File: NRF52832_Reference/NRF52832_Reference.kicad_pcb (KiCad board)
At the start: 2 copper layers, 47.5 x 35 mm, 24 parts, among them J1 MM8130-2600RA2, U1 NRF52810-QFAA, Y1 32MHz, Y2 32.768kHz

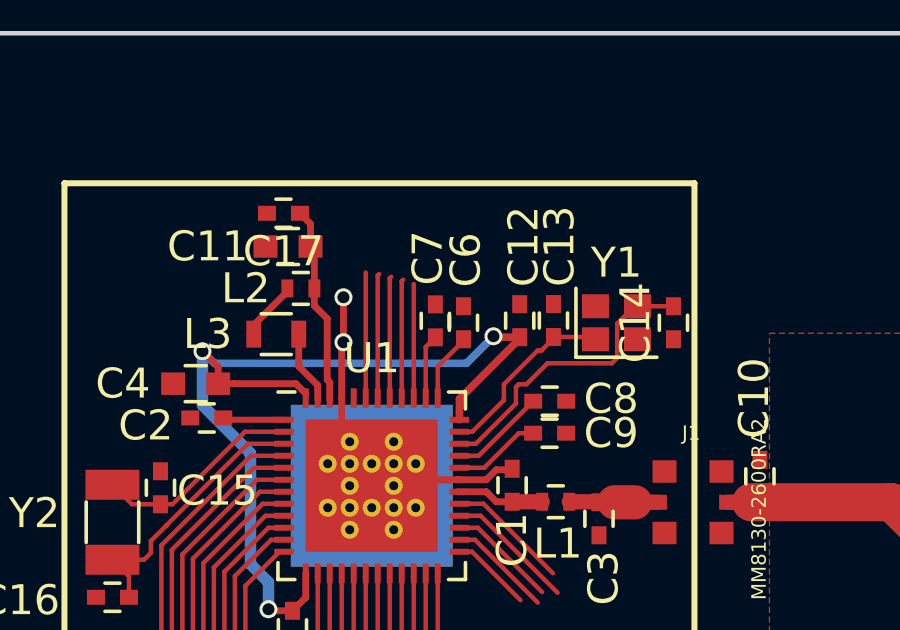
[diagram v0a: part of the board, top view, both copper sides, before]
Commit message: Removed unneeded capacitors from P0.25 and P0.26
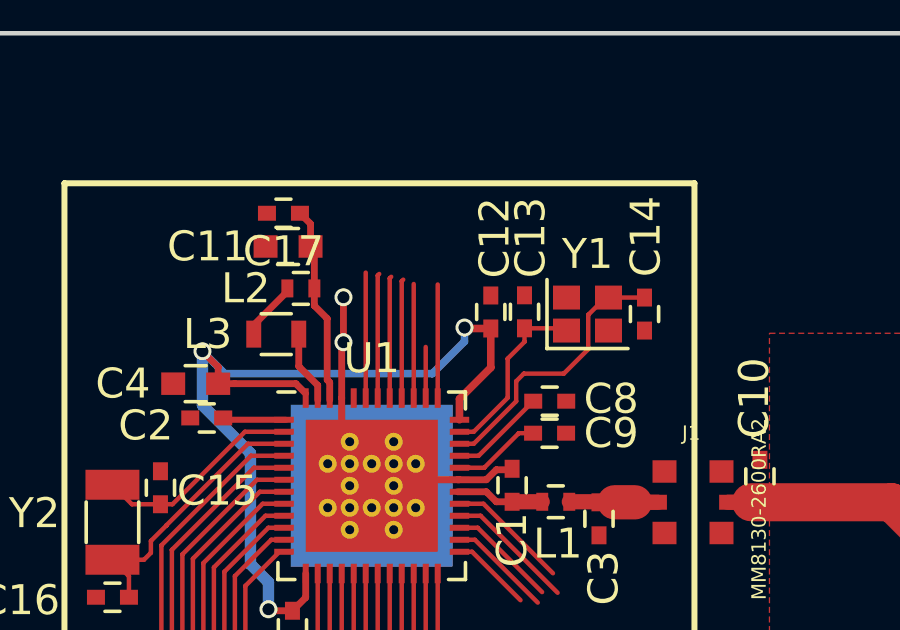
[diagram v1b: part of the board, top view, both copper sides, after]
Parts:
- removed C6, C7: 12pF, Capacitors_SMD:C_0402
- moved C12 1.01 mm to (145.7, 99.3)
- moved C13 1.01 mm to (146.8, 99.3)
- moved C14 1.01 mm to (150.8, 99.4)
- moved Y1 1.01 mm to (148.9, 99.4)
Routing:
- net Net-(U1-Pad37): track 2.38 -> 3.85 mm
- net Net-(C14-Pad2): track 10.1 -> 9.25 mm

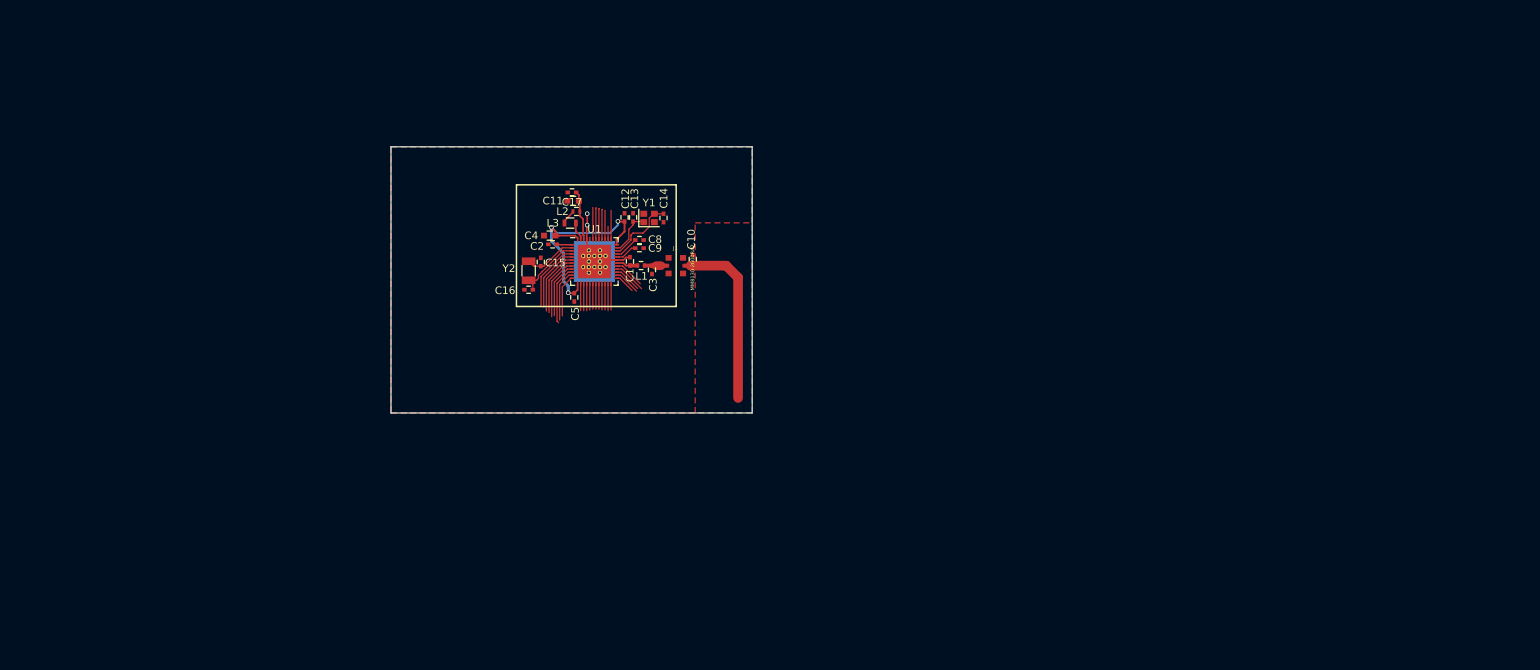
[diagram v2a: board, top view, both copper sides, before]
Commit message: Finished footprint assignments for NRF52 base components
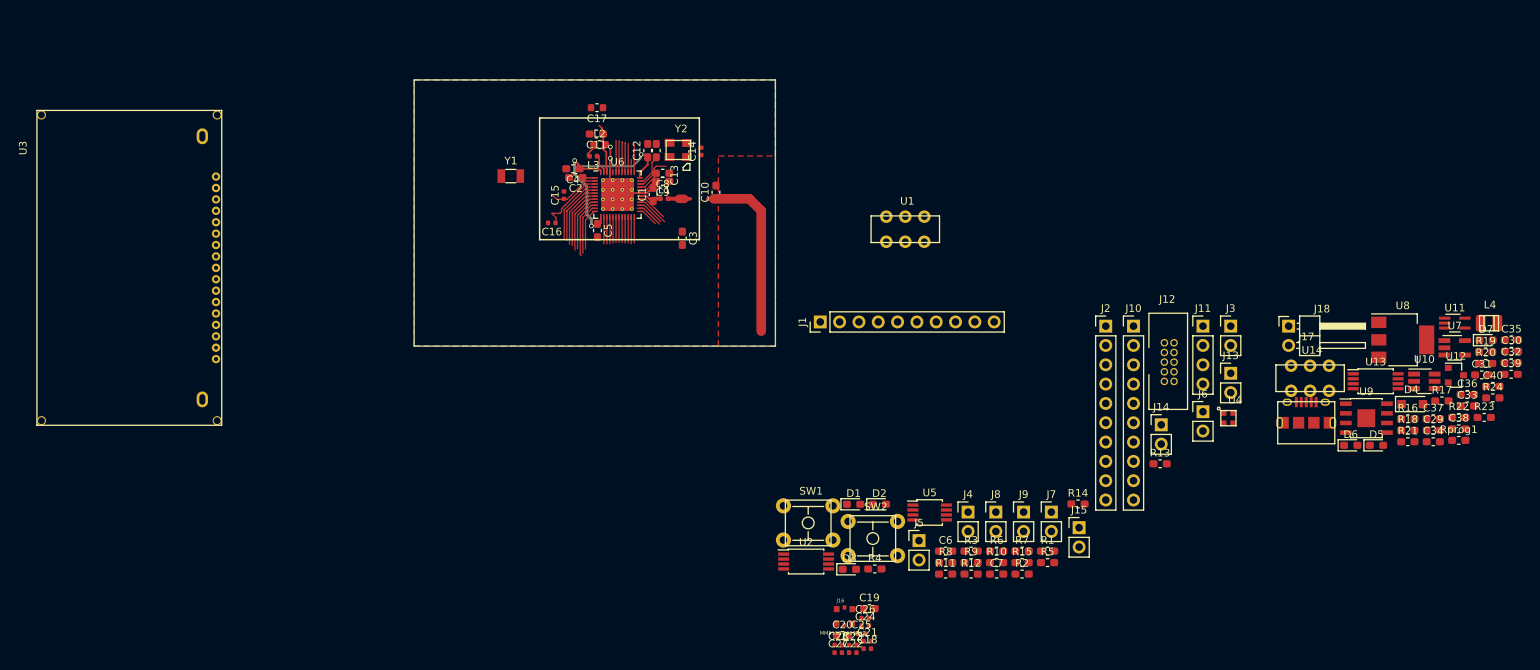
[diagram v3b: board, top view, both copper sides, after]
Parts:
- added C18: 100nF, Capacitor_SMD:C_0402_1005Metric, F.Cu at (177.6, 156.0)
- added C19: 1.0uF, Capacitor_SMD:C_0603_1608Metric, F.Cu at (177.9, 150.7)
- added C20: N.C., Capacitor_SMD:C_0603_1608Metric, F.Cu at (174.4, 154.3)
- added C21: 100nF, Capacitor_SMD:C_0402_1005Metric, F.Cu at (177.6, 155.0)
- added C22: 0.8pF, Capacitor_SMD:C_0402_1005Metric, F.Cu at (175.7, 156.5)
- added C23: 100pF, Capacitor_SMD:C_0402_1005Metric, F.Cu at (175.7, 155.5)
- added C24: N.C., Capacitor_SMD:C_0402_1005Metric, F.Cu at (177.4, 153.0)
- added C25: N.C., Capacitor_SMD:C_0402_1005Metric, F.Cu at (176.8, 154.0)
- added C26: 12pF, Capacitor_SMD:C_0402_1005Metric, F.Cu at (177.4, 152.0)
- added C27: 12nF, Capacitor_SMD:C_0402_1005Metric, F.Cu at (173.8, 156.5)
- added C28: 1.2pF, Capacitor_SMD:C_0402_1005Metric, F.Cu at (173.8, 155.5)
- added C29: 0.1uF, Capacitor_SMD:C_0603_1608Metric_Pad1.05x0.95mm_HandSolder, F.Cu at (252.1, 127.3)
- added C30: 4.7uF, Capacitor_SMD:C_0603_1608Metric_Pad1.05x0.95mm_HandSolder, F.Cu at (262.3, 116.9)
- added C31: 120pF, Capacitor_SMD:C_0603_1608Metric_Pad1.05x0.95mm_HandSolder, F.Cu at (258.4, 120.0)
- added C32: 10uF, Capacitor_SMD:C_0603_1608Metric_Pad1.05x0.95mm_HandSolder, F.Cu at (262.3, 118.4)
- added C33: 10uF, Capacitor_SMD:C_0603_1608Metric_Pad1.05x0.95mm_HandSolder, F.Cu at (256.5, 124.1)
- added C34: 4.7uF, Capacitor_SMD:C_0603_1608Metric_Pad1.05x0.95mm_HandSolder, F.Cu at (252.1, 128.8)
- added C35: 10uF, Capacitor_SMD:C_0603_1608Metric_Pad1.05x0.95mm_HandSolder, F.Cu at (262.3, 115.4)
- added C36: 0.1uF, Capacitor_SMD:C_0603_1608Metric_Pad1.05x0.95mm_HandSolder, F.Cu at (256.5, 122.6)
- added C37: 10uF, Capacitor_SMD:C_0603_1608Metric_Pad1.05x0.95mm_HandSolder, F.Cu at (252.1, 125.8)
- added C38: 1uF, Capacitor_SMD:C_0603_1608Metric_Pad1.05x0.95mm_HandSolder, F.Cu at (255.4, 127.1)
- added C39: 4.7uF, Capacitor_SMD:C_0603_1608Metric_Pad1.05x0.95mm_HandSolder, F.Cu at (262.3, 119.9)
- added C40: 10uF, Capacitor_SMD:C_0603_1608Metric_Pad1.05x0.95mm_HandSolder, F.Cu at (259.9, 121.5)
- added C6: 1uF, Capacitor_SMD:C_0603_1608Metric_Pad1.05x0.95mm_HandSolder, F.Cu at (187.9, 143.2)
- added C7: 1uF, Capacitor_SMD:C_0603_1608Metric_Pad1.05x0.95mm_HandSolder, F.Cu at (194.6, 146.2)
- added D1: LED, LED_SMD:LED_0603_1608Metric_Pad1.05x0.95mm_HandSolder, F.Cu at (175.8, 137.0)
- added D2: LED, LED_SMD:LED_0603_1608Metric_Pad1.05x0.95mm_HandSolder, F.Cu at (179.2, 137.0)
- added D3: LED, LED_SMD:LED_0603_1608Metric_Pad1.05x0.95mm_HandSolder, F.Cu at (175.3, 145.6)
- added D4: D_Schottky, Diode_SMD:D_SOD-123F, F.Cu at (249.3, 123.8)
- added D5: LED, LED_SMD:LED_0603_1608Metric_Pad1.05x0.95mm_HandSolder, F.Cu at (244.6, 129.3)
- added D6: LED, LED_SMD:LED_0603_1608Metric_Pad1.05x0.95mm_HandSolder, F.Cu at (241.2, 129.3)
- added D7: LED, LED_SMD:LED_0603_1608Metric_Pad1.05x0.95mm_HandSolder, F.Cu at (259.0, 115.4)
- added J10: Conn_01x10_Male, Connector_PinHeader_2.54mm:PinHeader_1x10_P2.54mm_Vertical, F.Cu at (212.6, 113.6)
- added J11: Conn_01x04_Male, Connector_PinHeader_2.54mm:PinHeader_1x04_P2.54mm_Vertical, F.Cu at (221.8, 113.6)
- added J12: SWD_Header, Custom_Footprints:SWD_Header_CNC_Tech_3220-10-0100-00, F.Cu at (216.7, 115.8)
- added J13: Conn_01x02_Male, Connector_PinHeader_2.54mm:PinHeader_1x02_P2.54mm_Vertical, F.Cu at (225.4, 119.8)
- added J14: Conn_01x02_Male, Connector_PinHeader_2.54mm:PinHeader_1x02_P2.54mm_Vertical, F.Cu at (216.3, 126.6)
- added J15: Conn_01x02_Male, Connector_PinHeader_2.54mm:PinHeader_1x02_P2.54mm_Vertical, F.Cu at (205.5, 140.1)
- added J16: MM8130-2600RA2, MM8130-2600RA2:MURATA_MM8130-2600RA2, F.Cu at (174.6, 151.7)
- added J17: USB_B_Micro, Custom_Footprints:USB_Micro_B_Amphenol_10118194-0001LF, F.Cu at (235.3, 126.3)
- added J18: Conn_01x02_Male, Connector_PinHeader_2.54mm:PinHeader_1x02_P2.54mm_Horizontal, F.Cu at (233.0, 113.6)
- added J2: Conn_01x10_Male, Connector_PinHeader_2.54mm:PinHeader_1x10_P2.54mm_Vertical, F.Cu at (209.0, 113.6)
- added J3: Conn_01x02_Male, Connector_PinHeader_2.54mm:PinHeader_1x02_P2.54mm_Vertical, F.Cu at (225.4, 113.6)
- added J4: Conn_01x02_Male, Connector_PinHeader_2.54mm:PinHeader_1x02_P2.54mm_Vertical, F.Cu at (190.9, 138.0)
- added J5: Conn_01x02_Male, Connector_PinHeader_2.54mm:PinHeader_1x02_P2.54mm_Vertical, F.Cu at (184.4, 141.8)
- added J6: Conn_01x02_Male, Connector_PinHeader_2.54mm:PinHeader_1x02_P2.54mm_Vertical, F.Cu at (221.8, 124.8)
- added J7: Conn_01x02_Male, Connector_PinHeader_2.54mm:PinHeader_1x02_P2.54mm_Vertical, F.Cu at (201.8, 138.0)
- added J8: Conn_01x02_Male, Connector_PinHeader_2.54mm:PinHeader_1x02_P2.54mm_Vertical, F.Cu at (194.5, 138.0)
- added J9: Conn_01x02_Male, Connector_PinHeader_2.54mm:PinHeader_1x02_P2.54mm_Vertical, F.Cu at (198.2, 138.0)
- added L4: 2.2uH, Custom_Footprints:L_1008_2520Metric, F.Cu at (259.4, 113.2)
- added R1: 10k, Resistor_SMD:R_0603_1608Metric_Pad1.05x0.95mm_HandSolder, F.Cu at (201.3, 143.2)
- added R10: 22, Resistor_SMD:R_0603_1608Metric_Pad1.05x0.95mm_HandSolder, F.Cu at (194.6, 144.7)
- added R11: 100, Resistor_SMD:R_0603_1608Metric_Pad1.05x0.95mm_HandSolder, F.Cu at (187.9, 146.2)
- added R12: 100, Resistor_SMD:R_0603_1608Metric_Pad1.05x0.95mm_HandSolder, F.Cu at (191.3, 146.2)
- added R13: 10k, Resistor_SMD:R_0603_1608Metric_Pad1.05x0.95mm_HandSolder, F.Cu at (216.1, 131.7)
- added R14: 22, Resistor_SMD:R_0603_1608Metric_Pad1.05x0.95mm_HandSolder, F.Cu at (205.3, 137.0)
- added R15: 22, Resistor_SMD:R_0603_1608Metric_Pad1.05x0.95mm_HandSolder, F.Cu at (198.0, 144.7)
- added R16: 10k, Resistor_SMD:R_0603_1608Metric_Pad1.05x0.95mm_HandSolder, F.Cu at (248.7, 125.8)
- added R17: 5.6, Resistor_SMD:R_0603_1608Metric_Pad1.05x0.95mm_HandSolder, F.Cu at (253.2, 123.4)
- added R18: 100, Resistor_SMD:R_0603_1608Metric_Pad1.05x0.95mm_HandSolder, F.Cu at (248.7, 127.3)
- added R19: 100k, Resistor_SMD:R_0603_1608Metric_Pad1.05x0.95mm_HandSolder, F.Cu at (258.9, 117.0)
- added R2: 10k, Resistor_SMD:R_0603_1608Metric_Pad1.05x0.95mm_HandSolder, F.Cu at (198.0, 146.2)
- added R20: 220k, Resistor_SMD:R_0603_1608Metric_Pad1.05x0.95mm_HandSolder, F.Cu at (258.9, 118.5)
- added R21: 300, Resistor_SMD:R_0603_1608Metric_Pad1.05x0.95mm_HandSolder, F.Cu at (248.7, 128.8)
- added R22: 1k, Resistor_SMD:R_0603_1608Metric_Pad1.05x0.95mm_HandSolder, F.Cu at (255.4, 125.6)
- added R23: 300, Resistor_SMD:R_0603_1608Metric_Pad1.05x0.95mm_HandSolder, F.Cu at (258.8, 125.6)
- added R24: 220, Resistor_SMD:R_0603_1608Metric_Pad1.05x0.95mm_HandSolder, F.Cu at (259.9, 123.0)
- added R3: 10k, Resistor_SMD:R_0603_1608Metric_Pad1.05x0.95mm_HandSolder, F.Cu at (191.3, 143.2)
- added R4: 10k, Resistor_SMD:R_0603_1608Metric_Pad1.05x0.95mm_HandSolder, F.Cu at (178.6, 145.5)
- added R5: 47k, Resistor_SMD:R_0603_1608Metric_Pad1.05x0.95mm_HandSolder, F.Cu at (201.3, 144.7)
- added R6: 47k, Resistor_SMD:R_0603_1608Metric_Pad1.05x0.95mm_HandSolder, F.Cu at (194.6, 143.2)
- added R7: 10k, Resistor_SMD:R_0603_1608Metric_Pad1.05x0.95mm_HandSolder, F.Cu at (198.0, 143.2)
- added R8: 100, Resistor_SMD:R_0603_1608Metric_Pad1.05x0.95mm_HandSolder, F.Cu at (187.9, 144.7)
- added R9: 10k, Resistor_SMD:R_0603_1608Metric_Pad1.05x0.95mm_HandSolder, F.Cu at (191.3, 144.7)
- added Rprog1: 1.2k, Resistor_SMD:R_0603_1608Metric_Pad1.05x0.95mm_HandSolder, F.Cu at (255.4, 128.6)
- added SW1: Button, Custom_Footprints:SW_Tactile_TE_1825910-6, F.Cu at (169.9, 139.5)
- added SW2: Button, Custom_Footprints:SW_Tactile_TE_1825910-6, F.Cu at (178.4, 141.5)
- added U10: DW01, Package_TO_SOT_SMD:SOT-23-6_Handsoldering, F.Cu at (250.9, 120.8)
- added U11: LMV331ICT, Package_TO_SOT_SMD:SOT-353_SC-70-5_Handsoldering, F.Cu at (254.9, 113.2)
- added U12: AP2138N-3.0TRG1, Package_TO_SOT_SMD:SOT-23, F.Cu at (255.0, 120.0)
- added U13: FS8205A, Package_SO:TSSOP-8_4.4x3mm_P0.65mm, F.Cu at (244.5, 120.8)
- added U14: SLIDE_SW_DPDT, Custom_Footprints:SW_DPDT_Slide_JS202011CQN, F.Cu at (235.9, 120.4)
- added U2: AT34C04-X5M-T, Package_SO:TSSOP-8_4.4x3mm_P0.65mm, F.Cu at (169.6, 144.5)
- added U3: NHD-C12832A1Z-NSW-BBW-3V3, Custom_Footprints:LCD_NHD-C12832A1Z-NSW-BBW-3V3, F.Cu at (80.6, 105.9)
- added U4: LTR-329ALS-01, Custom_Footprints:Sensor_Photo_LTR-329ALS-01, F.Cu at (225.1, 125.7)
- added U5: TCN75AVUA713, Package_SO:MSOP-8_3x3mm_P0.65mm, F.Cu at (185.8, 138.1)
- added U6: nRF52832, Package_DFN_QFN:QFN-48-1EP_6x6mm_P0.4mm_EP4.3x4.3mm_ThermalVias, F.Cu at (144.8, 96.3)
- added U7: TPS613222ADBVR, Package_TO_SOT_SMD:SOT-23-5_HandSoldering, F.Cu at (254.9, 116.4)
- added U8: AP2114HA-3.3TRG1, Package_TO_SOT_SMD:SOT-223-3_TabPin2, F.Cu at (248.0, 115.4)
- added U9: TP4056E-SN2L1P, Package_SO:SOIC-8-1EP_3.9x4.9mm_P1.27mm_EP2.35x2.35mm, F.Cu at (243.3, 125.7)
- C1: value 0.8pF -> 0.1uF; footprint Capacitors_SMD:C_0402 -> Capacitor_SMD:C_0603_1608Metric_Pad1.05x0.95mm_HandSolder
- C10: value 1.2pF -> 1uF; footprint Capacitors_SMD:C_0402 -> Capacitor_SMD:C_0603_1608Metric_Pad1.05x0.95mm_HandSolder
- C11: value 1.0uF -> 1uF; footprint Capacitors_SMD:C_0603 -> Capacitor_SMD:C_0603_1608Metric_Pad1.05x0.95mm_HandSolder
- C12: value 100nF -> 0.1uF; footprint Capacitors_SMD:C_0402 -> Capacitor_SMD:C_0603_1608Metric_Pad1.05x0.95mm_HandSolder
- C13: value 12pF -> 0.1uF; footprint Capacitors_SMD:C_0402 -> Capacitor_SMD:C_0603_1608Metric_Pad1.05x0.95mm_HandSolder
- C14: value 12nF -> 14pF; footprint Capacitors_SMD:C_0402 -> Capacitor_SMD:C_0402_1005Metric
- C15: value 12pF -> 14pF; footprint Capacitors_SMD:C_0402 -> Capacitor_SMD:C_0402_1005Metric
- C16: value 12pF -> 100nF; footprint Capacitors_SMD:C_0402 -> Capacitor_SMD:C_0402_1005Metric
- C17: value N.C. -> 4.7uF; footprint Capacitors_SMD:C_0402 -> Capacitor_SMD:C_0603_1608Metric
- C2, C5: value 100nF -> 1uF; footprint Capacitors_SMD:C_0402 -> Capacitor_SMD:C_0603_1608Metric_Pad1.05x0.95mm_HandSolder
- C3, C9: value N.C. -> 1uF; footprint Capacitors_SMD:C_0402 -> Capacitor_SMD:C_0603_1608Metric_Pad1.05x0.95mm_HandSolder
- C4: value 4.7uF -> 0.1uF; footprint Capacitors_SMD:C_0603 -> Capacitor_SMD:C_0603_1608Metric_Pad1.05x0.95mm_HandSolder
- C8: value 100pF -> 0.1uF; footprint Capacitors_SMD:C_0402 -> Capacitor_SMD:C_0603_1608Metric_Pad1.05x0.95mm_HandSolder
- J1: value MM8130-2600RA2 -> Conn_01x10_Male; footprint MM8130-2600RA2:MURATA_MM8130-2600RA2 -> Connector_PinHeader_2.54mm:PinHeader_1x10_P2.54mm_Vertical
- L1: value 3.9nH -> 15nH; footprint Inductors_SMD:L_0402 -> Inductor_SMD:L_0402_1005Metric
- L2: value 15nH -> 10uH; footprint Inductors_SMD:L_0402 -> Inductor_SMD:L_0603_1608Metric
- L3: value 10uH -> 3.9nH; footprint Inductors_SMD:L_0603 -> Inductor_SMD:L_0402_1005Metric
- U1: value NRF52810-QFAA -> SLIDE_SW_DPDT; footprint Package_DFN_QFN:QFN-48-1EP_6x6mm_P0.4mm_EP4.66x4.66mm_ThermalVias -> Custom_Footprints:SW_DPDT_Slide_JS202011CQN
- Y1: value 32MHz -> 32.768kHz; footprint Crystals:Crystal_SMD_2016-4pin_2.0x1.6mm -> Crystal:Crystal_SMD_3215-2Pin_3.2x1.5mm
- Y2: value 32.768kHz -> 32MHz; footprint Crystals:Crystal_SMD_3215-2pin_3.2x1.5mm -> Custom_Footprints:Crystal_32MHz_Kyocera_CX3225SB32000D0FFFCC
- moved U1 41.1 mm to (182.6, 100.8)
- moved Y2 25.3 mm to (152.8, 90.4), turned to 0 degrees
- moved J1 20.4 mm to (171.4, 113.0)
- moved Y1 19.0 mm to (130.8, 93.9)
- moved C17 11.6 mm to (142.1, 84.9)
- moved C14 10.1 mm to (155.8, 90.6)
- moved C10 9.30 mm to (157.7, 96.0)
- moved C11 9.30 mm to (142.0, 88.3)
- moved C12 9.30 mm to (148.8, 90.5)
- moved C13 9.30 mm to (149.9, 90.5), turned to 90 degrees
- moved C15 9.30 mm to (137.7, 96.4)
- moved C4 9.30 mm to (138.9, 92.9)
- moved C9 9.30 mm to (150.7, 94.5)
- moved L1 9.30 mm to (150.9, 96.8)
- moved C1 9.30 mm to (149.5, 96.3)
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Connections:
- C1 pad 1: GND -> 3V3_Ref
- C10 pad 1: /ANT -> Net-(C10-Pad1)
- C12 pad 1: VDD_nRF -> P0.24
- C13 pad 1: GND -> RESET
- C13 pad 2: Net-(C13-Pad2) -> GND
- C14 pad 1: GND -> Net-(C14-Pad1)
- C14 pad 2: Net-(C14-Pad2) -> GND
- C17 pad 1: Net-(C11-Pad1) -> 3V3_Ref
- C2 pad 2: GND -> Net-(C2-Pad2)
- C3 pad 1: /RF -> Net-(C3-Pad1)
- C3 pad 2: GND -> Net-(C3-Pad2)
- C4 pad 1: VDD_nRF -> 3V3_Ref
- C5 pad 1: VDD_nRF -> Net-(C5-Pad1)
- C8 pad 1: GND -> 3V3_Ref
- C8 pad 2: Net-(C8-Pad2) -> GND
- C9 pad 1: GND -> Net-(C9-Pad1)
- C9 pad 2: Net-(C9-Pad2) -> GND
- L1 pad 1: GND -> Net-(L1-Pad1)
- L1 pad 2: /RF -> Net-(C19-Pad1)
- L2 pad 2: Net-(C11-Pad1) -> Net-(L1-Pad1)
- L3 pad 1: Net-(L3-Pad1) -> Net-(C22-Pad1)
- L3 pad 2: Net-(L2-Pad1) -> /Sheet5BF15571/RF
- U1 pad 1: Net-(C2-Pad1) -> 3V_Ref
- U1 pad 2: Net-(C15-Pad1) -> Net-(U1-Pad2)
- U1 pad 3: Net-(C16-Pad1) -> Net-(U1-Pad3)
- U1 pad 4: Net-(U1-Pad4) -> 3V3_Ref
- Y1 pad 1: Net-(C13-Pad2) -> Net-(C14-Pad1)
- Y1 pad 2: GND -> Net-(C15-Pad1)
- Y2 pad 1: Net-(C15-Pad1) -> Net-(C26-Pad2)
- Y2 pad 2: Net-(C16-Pad1) -> GND
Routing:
- net /ANT: track 23.9 -> 0.00 mm
- net Net-(C10-Pad1): track 0.00 -> 23.9 mm
- net Net-(C14-Pad2): track 9.25 -> 0.00 mm
- net P0.02: track 0.00 -> 9.22 mm
- net Net-(U1-Pad4): track 9.22 -> 0.00 mm
- net P0.03: track 0.00 -> 8.82 mm
- net P0.04: track 0.00 -> 8.71 mm
- net Net-(U1-Pad6): track 8.71 -> 0.00 mm
- net P0.05: track 0.00 -> 8.31 mm
- net Net-(U1-Pad7): track 8.31 -> 0.00 mm
- net P0.06_CS1: track 0.00 -> 8.25 mm
- net Net-(U1-Pad8): track 8.25 -> 0.00 mm
- net Net-(U1-Pad10): track 7.92 -> 0.00 mm
- net P0.08_A0: track 0.00 -> 7.92 mm
- net P0.07_RES: track 0.00 -> 7.51 mm
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
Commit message: Updated component placement for PCB layout
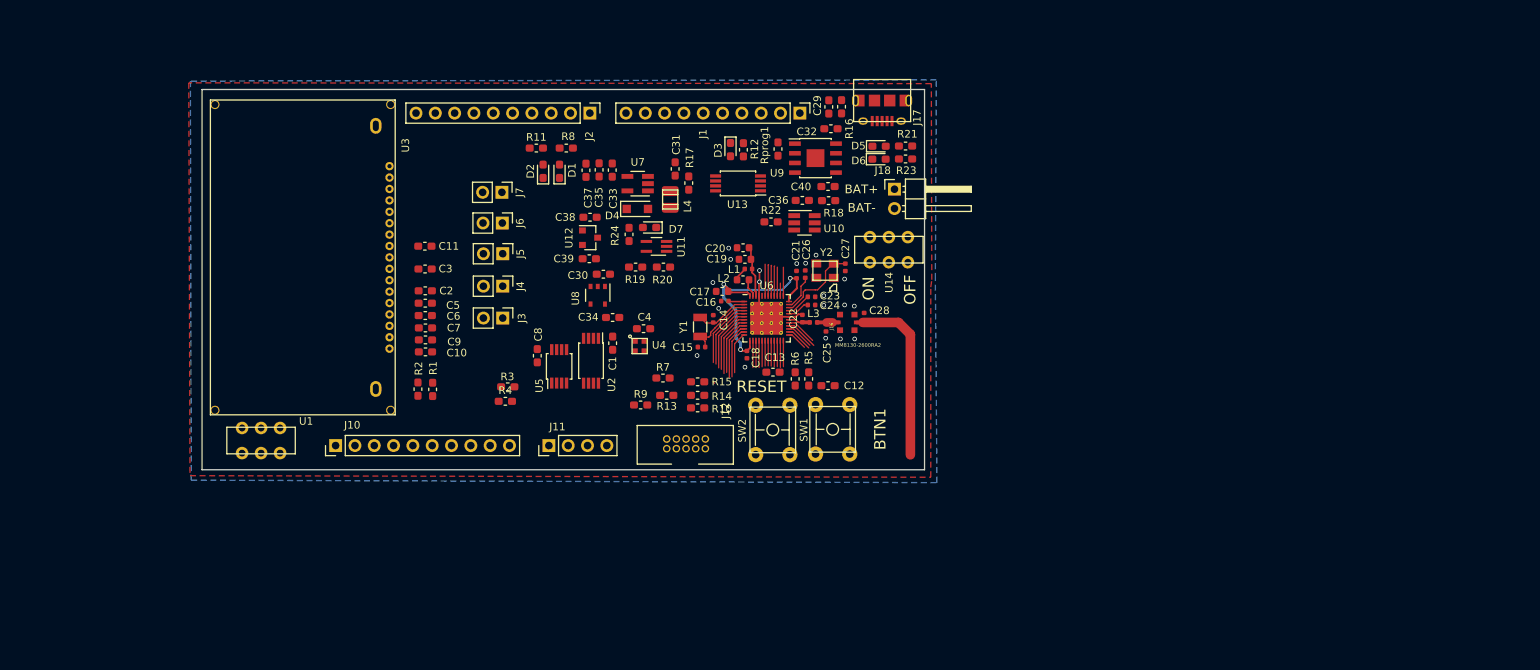
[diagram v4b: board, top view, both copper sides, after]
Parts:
- removed J13, J14, J15, J8, J9: Conn_01x02_Male, Connector_PinHeader_2.54mm:PinHeader_1x02_P2.54mm_Vertical
- C30, C34: value 4.7uF -> 1uF
- R3, R4: value 10k -> 4.7k
- U8: value AP2114HA-3.3TRG1 -> NCV8161BSN330T1G; footprint Package_TO_SOT_SMD:SOT-223-3_TabPin2 -> Package_SO:TSOP-5_1.65x3.05mm_P0.95mm
- moved C39 122.2 mm to (141.1, 104.7)
- moved C35 122.0 mm to (142.4, 93.0), turned to 90 degrees
- moved C30 119.8 mm to (142.9, 106.8), turned to 180 degrees
- moved C38 117.6 mm to (141.2, 99.3), turned to 180 degrees
- moved C33 116.6 mm to (144.1, 93.1), turned to 90 degrees
- moved C37 116.1 mm to (140.6, 93.1), turned to 90 degrees
- moved R24 115.6 mm to (146.3, 101.5), turned to 90 degrees
- moved U12 115.3 mm to (141.2, 102.0)
- moved R19 112.3 mm to (147.2, 105.8)
- moved D7 111.0 mm to (149.0, 100.6), turned to 180 degrees
- moved U7 109.6 mm to (147.4, 94.8), turned to 180 degrees
- moved C31 109.5 mm to (152.4, 92.9), turned to 270 degrees
- moved C34 109.1 mm to (144.1, 112.4)
- moved L4 108.9 mm to (151.7, 96.9), turned to 90 degrees
- moved R20 108.9 mm to (150.8, 105.8)
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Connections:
- J18 pad 1: Net-(C36-Pad2) -> Net-(C40-Pad1)
- J18 pad 2: Net-(C40-Pad1) -> Net-(C36-Pad2)
- R11 pad 1: Net-(J14-Pad1) -> P0.22
- R3 pad 2: Net-(J9-Pad2) -> P0.11_SDA
- R4 pad 2: Net-(J8-Pad2) -> P0.12_SCL
- R8 pad 1: Net-(J13-Pad1) -> P0.23
- U14 pad 1: Net-(C40-Pad1) -> Net-(U14-Pad1)
- U14 pad 2: V+ -> Net-(C40-Pad1)
- U14 pad 3: Net-(U14-Pad3) -> V+
- U2 pad 5: Net-(J9-Pad2) -> P0.11_SDA
- U2 pad 6: Net-(J8-Pad2) -> P0.12_SCL
- U4 pad 3: Net-(J9-Pad2) -> P0.11_SDA
- U4 pad 4: Net-(J8-Pad2) -> P0.12_SCL
- U5 pad 1: Net-(J9-Pad2) -> P0.11_SDA
- U5 pad 2: Net-(J8-Pad2) -> P0.12_SCL
- U8 pad 3: 3V3_Ref -> 5V_Ref
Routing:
- net 3V3_Ref: track 0.21 -> 30.9 mm, vias 0 -> 3
- net VDD_nRF: track 30.5 -> 0.00 mm, vias 3 -> 0
- net Net-(C10-Pad1): track 23.9 -> 0.00 mm
- net /Sheet5BF15571/ANT: track 0.00 -> 23.9 mm
- net Net-(C27-Pad2): track 0.00 -> 11.0 mm
- net GND: track 18.3 -> 9.18 mm, vias 0 -> 19
- net Net-(C16-Pad1): track 9.50 -> 2.11 mm
- net Net-(C14-Pad1): track 0.00 -> 7.05 mm
- net Net-(C11-Pad1): track 6.63 -> 0.00 mm
- net Net-(R1-Pad1): track 4.95 -> 0.00 mm, vias 2 -> 0
- net Net-(C19-Pad1): track 2.99 -> 7.01 mm
- net Net-(C23-Pad2): track 0.00 -> 3.28 mm
- net /Sheet5BF15571/RF: track 0.00 -> 3.14 mm
- net Net-(C24-Pad2): track 0.00 -> 3.00 mm
- net Net-(C15-Pad1): track 7.05 -> 9.50 mm
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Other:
- board size 47.5 x 35 mm -> 95 x 50 mm
- net class Default: clearance 0.2 -> 0.15; trace_width 0.25 -> 0.15
- rule trace_clearance: 0.2 -> 0.15
- board text added: "BAT+"
- board text added: "BAT-"
- board text added: "BTN1"
- board text added: "OFF"
- board text added: "ON"
- board text added: "RESET"

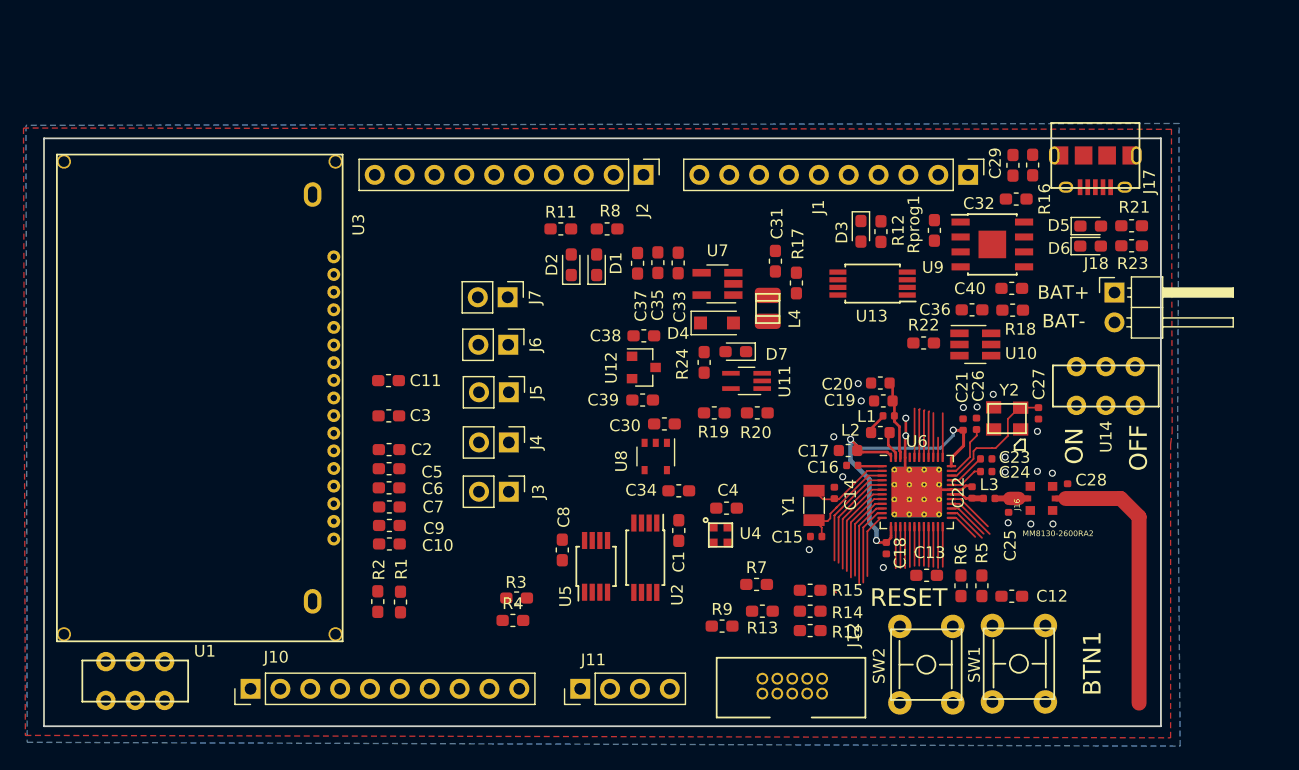
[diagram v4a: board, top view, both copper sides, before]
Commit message: Finished component placement on PCB layout. Ready for routing.
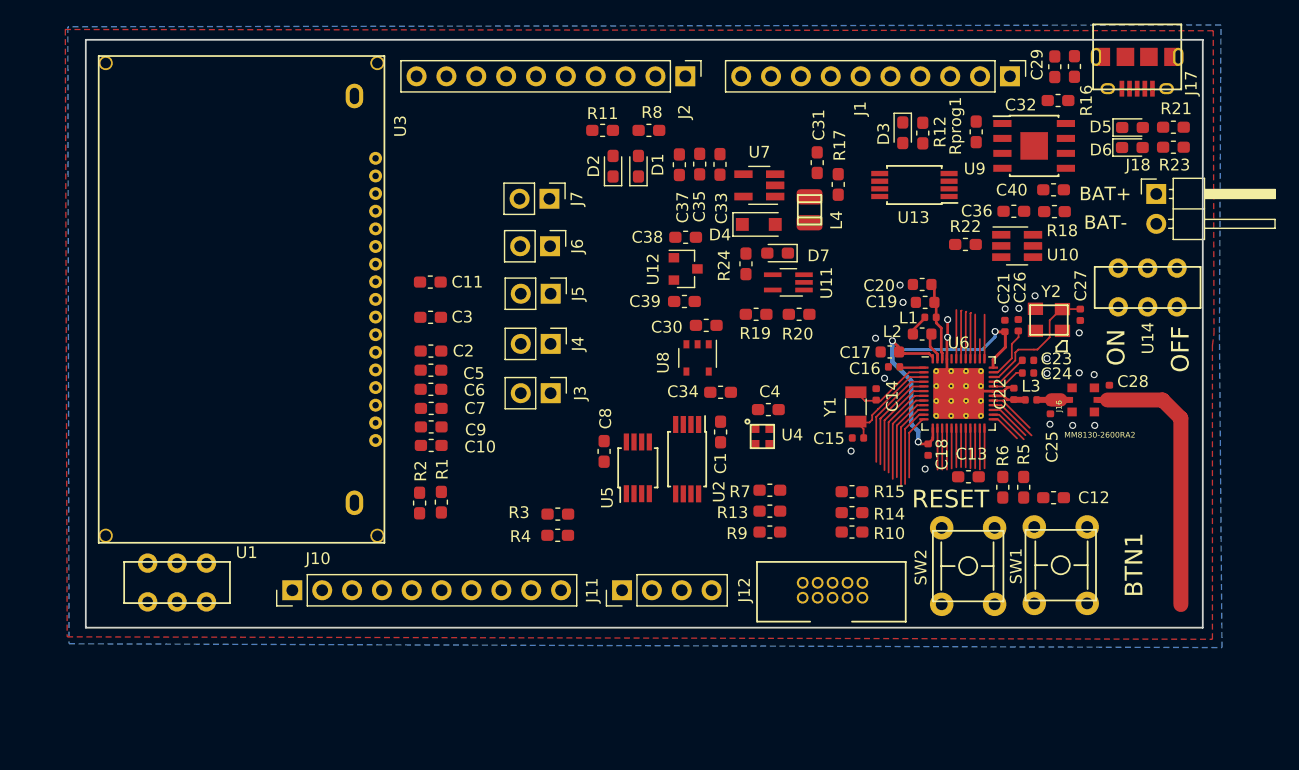
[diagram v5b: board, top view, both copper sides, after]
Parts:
- moved R1 9.18 mm to (124.0, 113.4)
- moved C11 9.11 mm to (123.0, 94.7)
- moved C16 9.11 mm to (162.5, 101.9)
- moved C17 9.11 mm to (162.1, 100.6)
- moved C18 9.11 mm to (165.4, 108.9)
- moved C21 9.11 mm to (171.9, 98.4)
- moved C24 9.11 mm to (173.9, 102.4)
- moved C25 9.11 mm to (175.8, 105.4)
- moved C27 9.11 mm to (178.3, 97.5)
- moved C28 9.11 mm to (180.8, 103.9)
- moved C29 9.11 mm to (176.1, 76.4)
- moved C31 9.11 mm to (155.9, 84.5)
- moved C33 9.11 mm to (147.7, 84.7)
- moved C35 9.11 mm to (145.9, 84.7)
- moved D1 9.11 mm to (140.7, 84.8)
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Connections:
- net /SWDCLK renamed Net-(J12-Pad4)
- net /SWDIO renamed Net-(J12-Pad2)
